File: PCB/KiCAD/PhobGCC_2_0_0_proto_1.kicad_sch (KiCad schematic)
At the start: 110 parts, among them J1 Conn_01x06_Female, J11 Conn_01x02, J14 Conn_01x06, J15 Conn_01x06, J2 Conn_01x02, J3 Conn_01x02, J4 Conn_01x01, J5 Rumble, J6 Conn_01x06, J8 USB_B_Micro, Q1 Q_NMOS_GSD, Q2 Q_PMOS_GDS, Q3 Q_NMOS_GSD, SW1 A, SW10 Dup, SW11 Dright, SW12 Ddown, SW2 B, SW3 X, SW4 Y, SW5 Start, SW6 L, SW7 R, SW8 Z, SW9 Dleft, U1 MCP3002, U10 DRV5055A2xDBZxQ1, U11 DRV5055A2xDBZxQ1, U12 USBLC6-2P6, U2 Stickbox_Assembly_Main, U3 MCP3002, U4 DRV5055A2xDBZxQ1, U5 Stickbox_Assembly_CStick, U6 AMS1117-3.3, U7 W25Q128JVS, U8 RP2040, U9 DRV5055A2xDBZxQ1, Y1 Crystal_GND24

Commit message: First commit of massive redesign
List of changes can be found in Din-Changes.txt
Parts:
- removed C1: C_Polarized, Capacitor_Tantalum_SMD:CP_EIA-3528-12_Kemet-T_Pad1.50x2.35mm_HandSolder, symbol Device:C_Polarized
- removed C14, C15: 27p, PhobGCC_2_0_0_footprints:C_0402_1005Metric, symbol Device:C
- removed C16, C18: 10u, PhobGCC_2_0_0_footprints:C_0805_2012Metric, symbol Device:C
- removed C17, C19, C20, C22, C24, C25, C26, C27, C28, C29, C30, C31, C32: 100n, PhobGCC_2_0_0_footprints:C_0402_1005Metric, symbol Device:C
- removed C21, C23: 1u, PhobGCC_2_0_0_footprints:C_0402_1005Metric, symbol Device:C
- removed C3, C4, C5, C6, C7, C8: 0.047u, PhobGCC_2_0_0_footprints:C_0603_HandSoldering, symbol Device:C
- removed D1: CUS10S30,H3F, Diode_SMD:D_SOD-323, symbol Diode:MBR0520
- removed D2: M7C, PhobGCC_2_0_0_footprints:D_SOD-123, symbol Device:D_Schottky
- removed D3, D4: D_Zener, Diode_SMD:D_SMA, symbol Device:D_Zener
- removed F1: Fuse, PhobGCC_2_0_0_footprints:Fuse_1206_3216Metric, symbol Device:Fuse
- removed H1: 5.2mm, PhobGCC_2_0_0_footprints:MountingHole_5.2mm, symbol Mechanical:MountingHole
- removed H10: MountingHole, PhobGCC_2_0_0_footprints:MountingHole_1.8mm, symbol Mechanical:MountingHole
- removed H11: MountingHole, PhobGCC_2_0_0_footprints:MountingHole_5.2mm, symbol Mechanical:MountingHole
- removed H12, H13: MountingHole, PhobGCC_2_0_0_footprints:MountingHole_2.0mm, symbol Mechanical:MountingHole
- removed H14: MouseBite, PhobGCC_2_0_0_footprints:breakaway-mousebites-double-v2-small, symbol Mechanical:MountingHole
- removed H15: MouseBite, PhobGCC_2_0_0_footprints:breakaway-mousebites-double-v2-large, symbol Mechanical:MountingHole
- removed H2: Slot, PhobGCC_2_0_0_footprints:Slot, symbol Mechanical:MountingHole
- removed H3, H4: 2mm, PhobGCC_2_0_0_footprints:MountingHole_2.0mm, symbol Mechanical:MountingHole
- removed H5, H6: 1.8mm, PhobGCC_2_0_0_footprints:MountingHole_1.8mm, symbol Mechanical:MountingHole
- removed H7: 2.4mm, PhobGCC_2_0_0_footprints:MountingHole_2.4mm, symbol Mechanical:MountingHole
- removed H8, H9: 2.2mm, PhobGCC_2_0_0_footprints:MountingHole_2.2mm, symbol Mechanical:MountingHole
- removed J11: Conn_01x02, PhobGCC_2_0_0_footprints:PinHeader_1x02_P2.00mm_Vertical, symbol Connector_Generic:Conn_01x02
- removed J6: Conn_01x06, Connector_PinSocket_2.00mm:PinSocket_1x06_P2.00mm_Vertical, symbol Connector_Generic:Conn_01x06
- removed Q1, Q3: Q_NMOS_GSD, PhobGCC_2_0_0_footprints:SOT-23, symbol Device:Q_NMOS_GSD
- removed Q2: Q_PMOS_GDS, PhobGCC_2_0_0_footprints:SOT-23, symbol Device:Q_PMOS_GSD
- removed R1, R2, R7, R8, R9: 180, PhobGCC_2_0_0_footprints:R_0402_1005Metric, symbol Device:R
- removed R10, R19, R24, R25: 316, PhobGCC_2_0_0_footprints:R_0402_1005Metric, symbol Device:R
- removed R11, R12: 100R, PhobGCC_2_0_0_footprints:R_0603_1608Metric_Pad0.98x0.95mm_HandSolder, symbol Device:R
- removed R13, R14, R15: 10k, PhobGCC_2_0_0_footprints:R_0603_1608Metric_Pad0.98x0.95mm_HandSolder, symbol Device:R
- removed R16, R18: 1k, PhobGCC_2_0_0_footprints:C_0402_1005Metric, symbol Device:R
- removed R20, R21: 27, PhobGCC_2_0_0_footprints:C_0402_1005Metric, symbol Device:R
- removed R3, R4, R5, R6: 2k, PhobGCC_2_0_0_footprints:R_0603_1608Metric_Pad0.98x0.95mm_HandSolder, symbol Device:R
- removed RV1, RV2: R_POT_MountingPin, PhobGCC_2_0_0_footprints:GCC_Slider, symbol GCC:Gamecube-MB-rescue_Slider_GCC-Gamecube_MB
- removed S1: BOOTSEL, PhobGCC_2_0_0_footprints:SW_TS-1187A-B-A-B, symbol TS-1187A-B-A-B:TS-1187A-B-A-B
- removed SW1: A, PhobGCC_2_0_0_footprints:ABXY_Contact_Omron_Switch_Circley, symbol Switch:SW_Push
- removed SW10: Dup, PhobGCC_2_0_0_footprints:Dpad_Contact_TL3315NF_2_ZigZag, symbol Switch:SW_Push
- removed SW11: Dright, PhobGCC_2_0_0_footprints:Dpad_Contact_TL3315NF_2_ZigZag, symbol Switch:SW_Push
- removed SW12: Ddown, PhobGCC_2_0_0_footprints:Dpad_Contact_TL3315NF_2_ZigZag, symbol Switch:SW_Push
- removed SW2: B, PhobGCC_2_0_0_footprints:ABXY_Contact_Omron_Switch_Circley, symbol Switch:SW_Push
- removed SW3: X, PhobGCC_2_0_0_footprints:ABXY_Contact_Omron_Switch_Circley, symbol Switch:SW_Push
- removed SW4: Y, PhobGCC_2_0_0_footprints:ABXY_Contact_Omron_Switch_Circley, symbol Switch:SW_Push
- removed SW5: Start, PhobGCC_2_0_0_footprints:Start_Contact, symbol Switch:SW_Push
- removed SW6: L, PhobGCC_2_0_0_footprints:Pin_Header_Straight_1x02_Pitch2.54mm, symbol Switch:SW_Push
- removed SW7: R, PhobGCC_2_0_0_footprints:Pin_Header_Straight_1x02_Pitch2.54mm, symbol Switch:SW_Push
- removed SW8: Z, PhobGCC_2_0_0_footprints:Z_Switch_Edge_Omron, symbol PhobGCC_Symbol_Library:SW_DIP_x01
- removed SW9: Dleft, PhobGCC_2_0_0_footprints:Dpad_Contact_TL3315NF_2_ZigZag, symbol Switch:SW_Push
- removed U1, U3: MCP3002, PhobGCC_2_0_0_footprints:SOIC-8_3.9x4.9mm_P1.27mm, symbol Analog_ADC:MCP3002
- removed U10, U11, U4, U9: DRV5055A2xDBZxQ1, PhobGCC_2_0_0_footprints:SOT-23, symbol Sensor_Magnetic:DRV5055A2xDBZxQ1
- removed U2: Stickbox_Assembly_Main, PhobGCC_2_0_0_footprints:GCC_Stickbox_Hall_Only, symbol GCC:Gamecube-MB-rescue_Stickbox_Assembly-Gamecube_MB
- removed U5: Stickbox_Assembly_CStick, PhobGCC_2_0_0_footprints:GCC_Stickbox_Hall_Only, symbol Gamecube MB:Stickbox_Assembly_Hall_Only
- removed U6: AMS1117-3.3, PhobGCC_2_0_0_footprints:SOT-223-3_TabPin2, symbol Regulator_Linear:AMS1117-3.3
- removed U7: W25Q128JVS, PhobGCC_2_0_0_footprints:SOIC-8_5.23x5.23mm_P1.27mm, symbol Memory_Flash:W25Q128JVS
- removed U8: RP2040, PhobGCC_2_0_0_footprints:RP2040-QFN-56, symbol MCU_RaspberryPi_RP2040:RP2040
- removed Y1: Crystal_GND24, PhobGCC_2_0_0_footprints:Crystal_SMD_3225-4Pin_3.2x2.5mm, symbol Device:Crystal_GND24
- added C13: C_Polarized, Capacitor_Tantalum_SMD:CP_EIA-3528-12_Kemet-T_Pad1.50x2.35mm_HandSolder, symbol Device:C_Polarized
- added FB1, FB2, FB3, FB5: FerriteBead_Small, Resistor_SMD:R_0805_2012Metric, symbol Device:FerriteBead_Small
- added FB4: FerriteBead_Small, Resistor_SMD:R_0603_1608Metric, symbol Device:FerriteBead_Small
- added J7: L, PhobGCC_2_0_0_footprints:Pin_Header_Straight_1x02_Pitch2.54mm, symbol Connector:Conn_01x02_Male
- added J9: R, PhobGCC_2_0_0_footprints:Pin_Header_Straight_1x02_Pitch2.54mm, symbol Connector:Conn_01x02_Male
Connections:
- net +3V3: now also C13.1, FB2.2; no longer J1.1 (Pin_1)
- net +5V: now also FB3.2; no longer J1.2 (Pin_2), J5.1 (Pin_1)
- net GCC_DATA: now also FB4.2; no longer J1.3 (Pin_3)
- net GND: now also C13.2, FB1.1; no longer J1.4 (Pin_4), J1.5 (Pin_5), J1.6 (Pin_6)
- net Rumble/Rumble-: now reaches J5.2 (Pin_2)
- new net: FB3.1, J1.2 (Pin_2)
- new net: FB2.1, J1.1 (Pin_1)
- new net: FB4.1, J1.3 (Pin_3)
- new net: FB5.1, J1.5 (Pin_5)
- new net: FB1.2, J1.4 (Pin_4), J1.6 (Pin_6)
- new net GNDPWR: FB5.2
- new net Rumble/Rumble+: J5.1 (Pin_1)
- new net TriggerPaddles/L+: J7.1 (Pin_1)
- new net TriggerPaddles/L-: J7.2 (Pin_2)
- new net TriggerPaddles/R+: J9.1 (Pin_1)
- new net TriggerPaddles/R-: J9.2 (Pin_2)
- no-connect marks 2 -> 1
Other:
- added sheet Buttons (Buttons.kicad_sch)
- added sheet Communications (Communications.kicad_sch)
- added sheet Flash (flash.kicad_sch)
- added sheet Microcontroller (Microcontroller.kicad_sch)
- added sheet Miscellaneous (Miscellaneous.kicad_sch)
- added sheet PhobVision (PhobVision.kicad_sch)
- added sheet PowerSupply (PowerSupply.kicad_sch)
- added sheet Rumble (Rumble.kicad_sch)
- added sheet Stickbox_CStick (Stickbox_CStick.kicad_sch)
- added sheet Stickbox_GrayStick (Stickbox_GrayStick.kicad_sch)
- added sheet TriggerPaddles (TriggerPaddles.kicad_sch)
- added sheet TriggerSliders (TriggerSliders.kicad_sch)
- note added: "GCC CABLE CONNECTOR"
- note added: "GND access for troubleshooting."
- note added: "U12 is close enough to USB connector and regulator that bypass likely unneeded."
- note added: "USB CONNECTOR"
- note removed: "CStick X"
- note removed: "CStick Y"
- note removed: "Crystal"
- note removed: "Flash"
- note removed: "LStick X"
- note removed: "LStick Y"
- note removed: "Make sure C10 is close to pin 44 of RP2040"
- note removed: "Make sure C8 is close to pin 45 of RP2040"
- note removed: "Make sure R3 and R4 are close to RP2040"
- note removed: "Power"
- title: (none) -> PHORAE

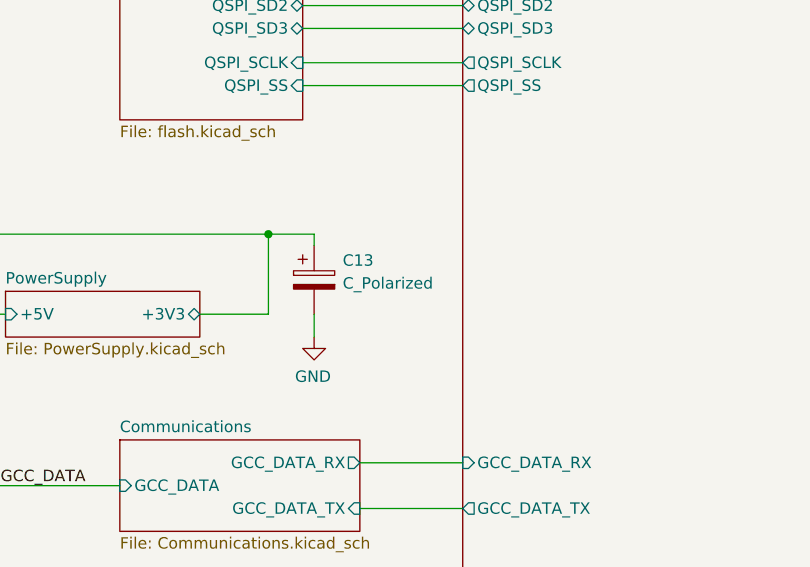
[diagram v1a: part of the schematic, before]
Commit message: Assembly and fab upload
Upload schematic pdf and bom csv and ibom html docs
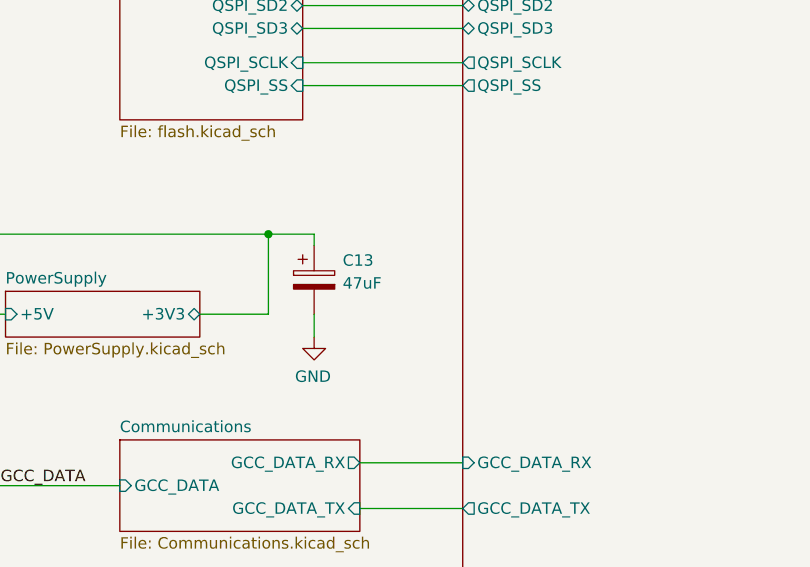
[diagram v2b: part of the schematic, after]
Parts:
- C13: value C_Polarized -> 47uF; MPN (none) -> GRM32ER71A476ME15L; Manufacturer (none) -> Murata Electronics; Package (none) -> 1210; VARIANT (none) -> NoVar
- FB1, FB2, FB3, FB5: MPN (none) -> 2508056017Y2; Manufacturer (none) -> Fair-Rite Products Corp.; Package (none) -> 0805; VARIANT (none) -> NoVar
- FB4: MPN (none) -> MMZ1608B601CTAH0; Manufacturer (none) -> TDK Corporation; Package (none) -> 0603; VARIANT (none) -> NoVar
- J1, J14, J15, J2, J3, J4, J7, J9: DNP (none) -> DNP; Package (none) -> Virtual; VARIANT (none) -> NoVar
- J5: DNP (none) -> DNP; Package (none) -> Mechanical; VARIANT (none) -> NoVar
- J8: MPN (none) -> 10118194-0001LF; Manufacturer (none) -> Amphenol ICC (FCI); Package (none) -> Hybrid; VARIANT (none) -> NoVar
- R17: MPN (none) -> RC0603FR-07100KL; Manufacturer (none) -> YAGEO; Package (none) -> 0603; VARIANT (none) -> NoVar
- U12: MPN (none) -> USBLC6-2P6; Manufacturer (none) -> STMicroelectronics; Package (none) -> SOT-666; VARIANT (none) -> NoVar
